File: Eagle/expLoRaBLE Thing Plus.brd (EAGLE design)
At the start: 22.9 x 58.4 mm, 132 parts, among them J2 CORTEX_DEBUG, J5 USB-C, J8 U.FL, U1 MCP73831, U2 3.3V, U3 NM180100, U4 CH340E_MSOP10, U6 DPX202700DT-4162A1, Y1 32.768kHz

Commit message: Create prelim board fabrication files
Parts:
- removed R10, R9: 10k, SparkFun-Resistors:0603
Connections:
- removed net LORA_EN: U3.J4
- net 3.3V: no longer R10.2, R9.2
- net D14/QWIIC_SDA: no longer R10.1
- net ~D15/QWIIC_SCL: no longer R9.1
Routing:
- net ~D15/QWIIC_SCL: track 45.8 -> 39.2 mm
- net D14/QWIIC_SDA: track 43.6 -> 39.4 mm
- net 3.3V: track 106.6 -> 103.5 mm
- net GND: vias 22 -> 27

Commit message: Made suggested changes
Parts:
- moved TP2 0.99 mm to (12.7, 36.8)
- moved TP3 0.80 mm to (15.2, 35.6)
- moved TP4 0.30 mm to (3.81, 7.62)
- moved TP5 0.21 mm to (2.54, 8.89)
- moved D5 0.08 mm to (14.4, 33.9)
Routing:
- net 3.3V: track 103.5 -> 42.6 mm, vias 10 -> 11
- added copper zone on layer 2, net 3.3V
- added copper zone on layer 15, net GND
- added copper zone on layer 2, net GND
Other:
- board text added: "v01"
- board text removed: "v10"

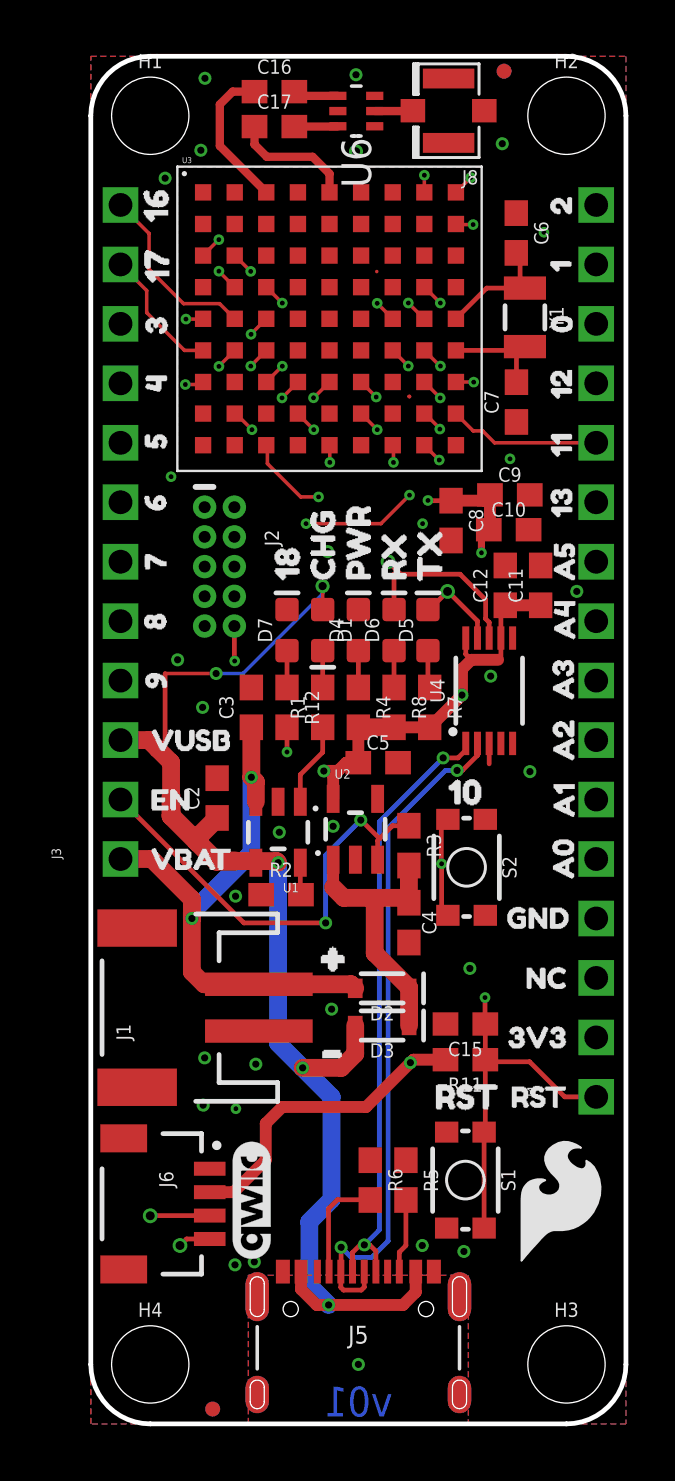
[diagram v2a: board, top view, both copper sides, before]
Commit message: TP and Jumper addition
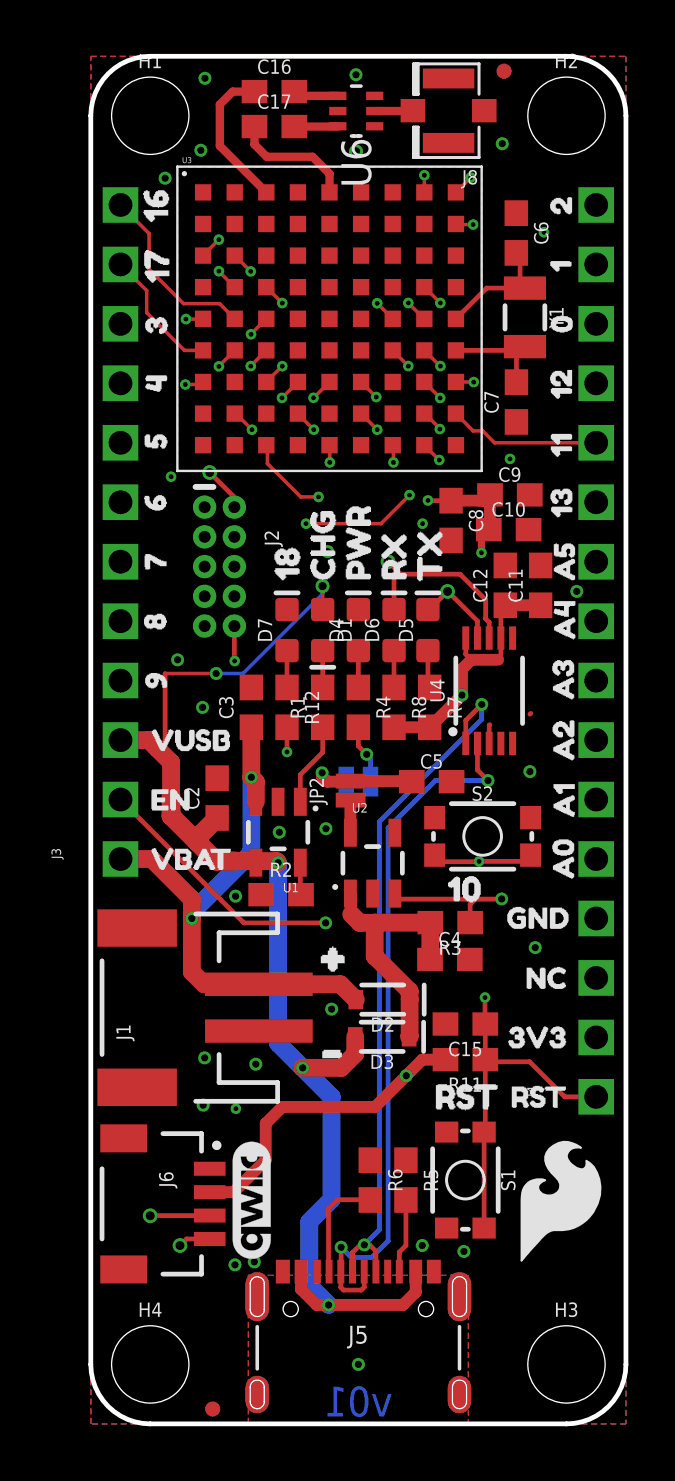
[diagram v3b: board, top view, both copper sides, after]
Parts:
- added JP1: JUMPER-SMT_2_NC_TRACE_NO-SILK, SparkFun-Jumpers:SMT-JUMPER_2_NC_TRACE_NO-SILK
- added JP2: JUMPER-SMT_2_NC_PASTE_NO-SILK, SparkFun-Jumpers:SMT-JUMPER_2_NC_PASTE_NO-SILK
- added TP1: TEST-POINTTP_15TH_THRU, SparkFun-Connectors:TP_15TH
- moved U$62 4.14 mm to (14.3, 22.9)
- moved R3 3.73 mm to (15.4, 21.4), turned to 180 degrees
- moved C5 2.43 mm to (14.6, 27.4)
- moved C4 2.36 mm to (15.3, 19.8), turned to 0 degrees
- moved U2 1.62 mm to (12.0, 24.0)
- moved S2 1.49 mm to (16.7, 25.1), turned to 0 degrees
- moved D2 0.48 mm to (12.5, 18.1)
- moved D3 0.48 mm to (12.4, 16.5)
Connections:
- new net N$14: JP2.1, U2.5
- new net N$6: JP1.1, R4.2
- net 3.3V: now also JP1.2, JP2.2; no longer R4.2, U2.5
- net SWDIO: now also TP1.P$1
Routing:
- net EN: track 19.5 -> 25.1 mm
- net D+1: track 26.5 -> 30.1 mm
- net N$6: track 0.00 -> 2.54 mm, vias 0 -> 1
- net SWDIO: track 7.52 -> 9.43 mm
- net D10/SWCH: track 26.1 -> 27.7 mm
- net N$14: track 0.00 -> 1.40 mm
- net D-1: track 29.2 -> 30.5 mm
- net !RESET: track 59.1 -> 59.9 mm
- net VIN: track 12.3 -> 11.5 mm
- net 3.3V: track 42.6 -> 42.0 mm
- net GND: track 0.92 -> 0.87 mm, vias 27 -> 26

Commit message: Updated labels to buzzard vectors and more minor tweaks
-also nudged some components near TX LED to make room for silk to avoid nearby mask.
-added version text object to both sch sheets
-redrew some sch to avoid 4-way nodes
-added buzzard label to bottom LED disable jumper
-moved ISO jumper to trace closed, added top silk label
-added special ordering instructions with 4-layer board text on tDocu
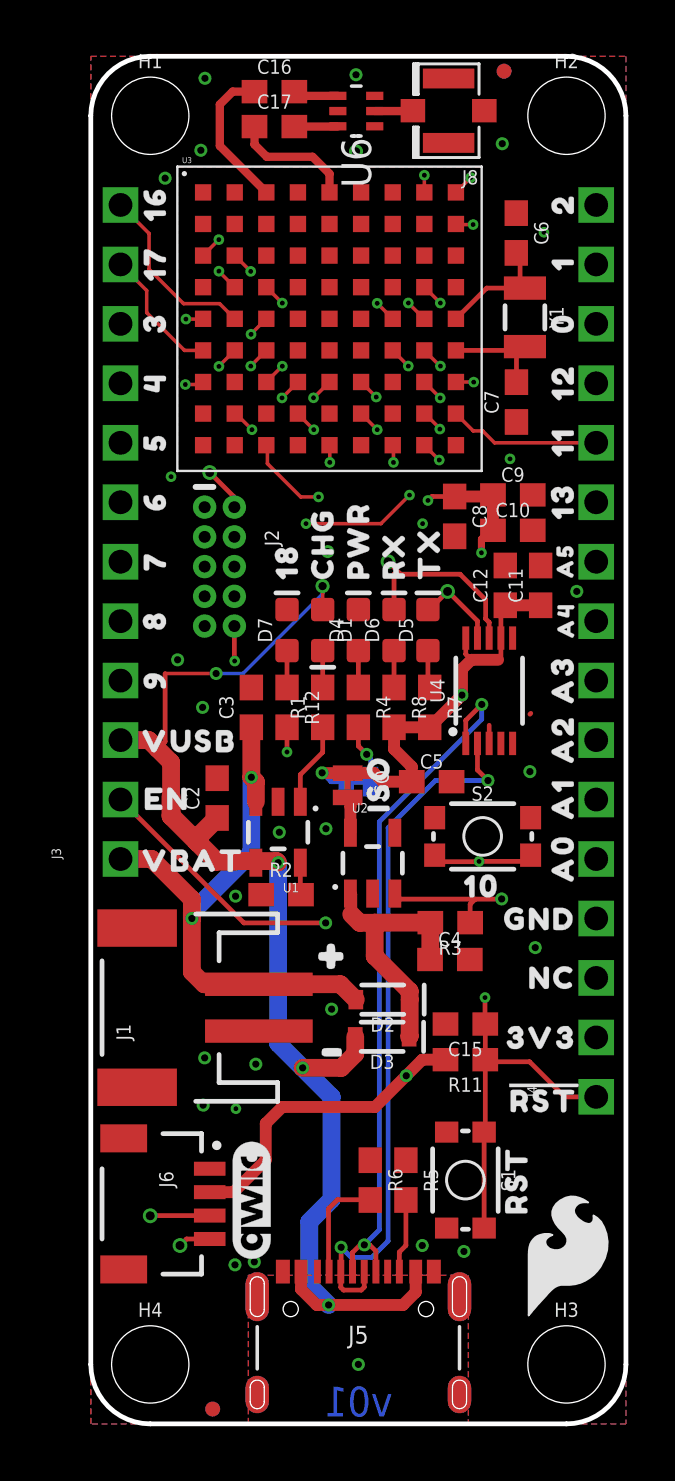
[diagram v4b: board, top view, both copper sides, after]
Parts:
- removed JP1: JUMPER-SMT_2_NC_TRACE_NO-SILK, SparkFun-Jumpers:SMT-JUMPER_2_NC_TRACE_NO-SILK
- removed JP2: JUMPER-SMT_2_NC_PASTE_NO-SILK, SparkFun-Jumpers:SMT-JUMPER_2_NC_PASTE_NO-SILK
- removed U$34: (no value), buzzard_labels (6):20
- removed U$35: (no value), buzzard_labels (6):1#TX11
- removed U$36: (no value), buzzard_labels (6):0#RX12
- removed U$37: (no value), buzzard_labels (6):12#MISO3
- removed U$38: (no value), buzzard_labels (6):11#MOSI4
- removed U$39: (no value), buzzard_labels (6):13#SCK5
- removed U$40: (no value), buzzard_labels (6):A56
- removed U$41: (no value), buzzard_labels (6):A47
- removed U$42: (no value), buzzard_labels (6):A38
- removed U$43: (no value), buzzard_labels (6):A29
- removed U$44: (no value), buzzard_labels (6):A110
- removed U$45: (no value), buzzard_labels (6):A011
- removed U$46: (no value), buzzard_labels (2):GND12
- removed U$47: (no value), buzzard_labels (2):NC13
- removed U$48: (no value), buzzard_labels (2):3V314
- removed U$49: (no value), buzzard_labels (2):#RESET15
- removed U$50: (no value), buzzard_labels (11):16#SDA12
- removed U$51: (no value), buzzard_labels (11):17#SCL13
- removed U$52: (no value), buzzard_labels (6):412
- removed U$53: (no value), buzzard_labels (6):513
- removed U$54: (no value), buzzard_labels (6):614
- removed U$55: (no value), buzzard_labels (6):715
- removed U$56: (no value), buzzard_labels (6):816
- removed U$57: (no value), buzzard_labels (6):9#A719
- removed U$58: (no value), buzzard_labels (7):3#A60
- removed U$59: (no value), buzzard_labels (2):VUSB25
- removed U$60: (no value), buzzard_labels (2):EN26
- removed U$61: (no value), buzzard_labels (2):VBAT27
- removed U$63: (no value), buzzard_labels (3):RST1
- added ISO: JUMPER-SMT_2_NC_TRACE_NO-SILK, SparkFun-Jumpers:SMT-JUMPER_2_NC_TRACE_NO-SILK
- added LED: JUMPER-SMT_2_NC_TRACE_SILK, SparkFun-Jumpers:SMT-JUMPER_2_NC_TRACE_SILK
- added LOGO4: SPECIAL_INSTRUCTIONS-ORDERING, SparkFun-Aesthetics:ORDERING_INSTRUCTIONS
- added U$100: (no value), output:RX0
- added U$101: (no value), output:TX0
- added U$66: (no value), output:160
- added U$69: (no value), output:170
- added U$70: (no value), output:30
- added U$71: (no value), output:40
- added U$72: (no value), output:50
- added U$73: (no value), output:60
- added U$74: (no value), output:70
- added U$75: (no value), output:80
- added U$76: (no value), output:90
- added U$78: (no value), output:EN0
- added U$79: (no value), output:VBAT0
- added U$80: (no value), output:20
- added U$81: (no value), output:10
- added U$82: (no value), output:00
- added U$83: (no value), output:120
- added U$84: (no value), output:110
- added U$85: (no value), output:130
- added U$86: (no value), output:A50
- added U$87: (no value), output:A40
- added U$88: (no value), output:A30
- added U$89: (no value), output:A20
- added U$90: (no value), output:A10
- added U$91: (no value), output:A00
- added U$92: (no value), output:GND0
- added U$93: (no value), output:NC0
- added U$94: (no value), output:3V30
- added U$95: (no value), output:#RST#0
- added U$96: (no value), output:RST0
- added U$97: (no value), output:100
- added U$98: (no value), output:#0
- added U$99: (no value), output:#_0
- U$1: device buzzard_labels (11):160 -> output:#16#SDA1#0
- U$10: device buzzard_labels:VUSB9 -> output:#8#0
- U$11: device buzzard_labels:EN10 -> output:#9#A7#0
- U$12: device buzzard_labels:VBAT11 -> output:#VUSB#0
- U$13: device buzzard_labels:227 -> output:VUSB0
- U$14: device buzzard_labels:126 -> output:#EN#0
- U$15: device buzzard_labels:025 -> output:#VBAT#0
- U$16: device buzzard_labels:1123 -> output:#2#0
- U$17: device buzzard_labels:1224 -> output:#1#TX1#0
- U$18: device buzzard_labels:1322 -> output:#0#RX1#0
- U$19: device buzzard_labels:A521 -> output:#12#CIPO#0
- U$2: device buzzard_labels (11):171 -> output:LORA_THING_PLUS0
- U$20: device buzzard_labels:A420 -> output:#11#COPI#0
- U$21: device buzzard_labels:A319 -> output:#13#SCK#0
- U$22: device buzzard_labels:A218 -> output:#A5#0
- U$23: device buzzard_labels:A117 -> output:#A4#0
- U$24: device buzzard_labels:A016 -> output:#A3#0
- U$25: device buzzard_labels:GND13 -> output:#A2#0
- U$26: device buzzard_labels:NC12 -> output:#A1#0
- U$27: device buzzard_labels:3V314 -> output:#A0#0
- U$28: device buzzard_labels:RST15 -> output:#GND#0
- U$29: device buzzard_labels (11):184 -> output:#NC#0
- U$3: device buzzard_labels:32 -> output:EXPLORABLE0
- U$30: device buzzard_labels (1):CHG1 -> output:#3V3#0
- U$31: device buzzard_labels (1):PWR2 -> output:##RESET##0
- U$32: device buzzard_labels (1):RX3 -> output:#LED#0
- U$33: device buzzard_labels (1):TX4 -> output:ISO0
- U$4: device buzzard_labels:43 -> output:#17#SCL1#0
- U$5: device buzzard_labels:54 -> output:#3#A6#0
- U$6: device buzzard_labels:65 -> output:#4#0
- U$62: device buzzard_labels (3):100 -> output:180
- U$67: device buzzard_labels (13):#0 -> output:CHG0
- U$68: device buzzard_labels (13):#1 -> output:PWR0
- U$7: device buzzard_labels:76 -> output:#5#0
- U$8: device buzzard_labels:87 -> output:#6#0
- U$9: device buzzard_labels:98 -> output:#7#0
- moved U$3 40.3 mm to (11.4, 6.35), flipped to the bottom, turned to 0 degrees
- moved U$2 39.9 mm to (11.4, 8.89), flipped to the bottom, turned to 0 degrees
- moved LOGO1 37.5 mm to (11.4, 55.2), turned to 0 degrees
- moved U$14 28.4 mm to (1.75, 26.7), flipped to the bottom, turned to 0 degrees
- moved U$15 28.4 mm to (1.75, 24.1), flipped to the bottom, turned to 0 degrees
- moved U$13 26.9 mm to (4.22, 29.2), turned to 0 degrees
- moved U$31 23.3 mm to (21.1, 14.0), flipped to the bottom, turned to 0 degrees
- moved U$68 21.8 mm to (11.4, 37.7), turned to 90 degrees
- moved U$30 21.7 mm to (21.1, 16.5), flipped to the bottom, turned to 0 degrees
- moved U$29 20.5 mm to (21.1, 19.1), flipped to the bottom, turned to 0 degrees
- moved LOGO3 20.3 mm to (17.3, 9.46), turned to 0 degrees
- moved U$67 17.6 mm to (9.91, 37.6), turned to 90 degrees
- moved U$62 15.2 mm to (8.38, 36.8), turned to 90 degrees
- moved U$16 11.6 mm to (21.1, 52.1), flipped to the bottom, turned to 0 degrees
- moved U$22 9.48 mm to (21.1, 36.8), flipped to the bottom, turned to 0 degrees
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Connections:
- net 3.3V: now also ISO.1, LED.2; no longer JP1.2, JP2.2
- net N$14: now also ISO.2; no longer JP2.1
- net N$6: now also LED.1; no longer JP1.1
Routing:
- net 3.3V: track 42.0 -> 44.6 mm
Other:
- board text added: "4-LAYER BOARD"
